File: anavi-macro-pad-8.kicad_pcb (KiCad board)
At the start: 2 copper layers, 40 parts, among them J1 USB_B_Micro, J2 Conn_01x04_Female, J3 Conn_01x03_Male, J4 Conn_01x03_Male, Q1 Q_NPN_BEC, SW1 SW_DIP_x01, SW2 SW_DIP_x01, SW3 SW_DIP_x01, SW4 SW_DIP_x01, SW5 SW_DIP_x01, SW6 SW_DIP_x01, SW7 SW_DIP_x01, SW8 SW_DIP_x01, U1 ATmega32U4-AU, Y1 Crystal

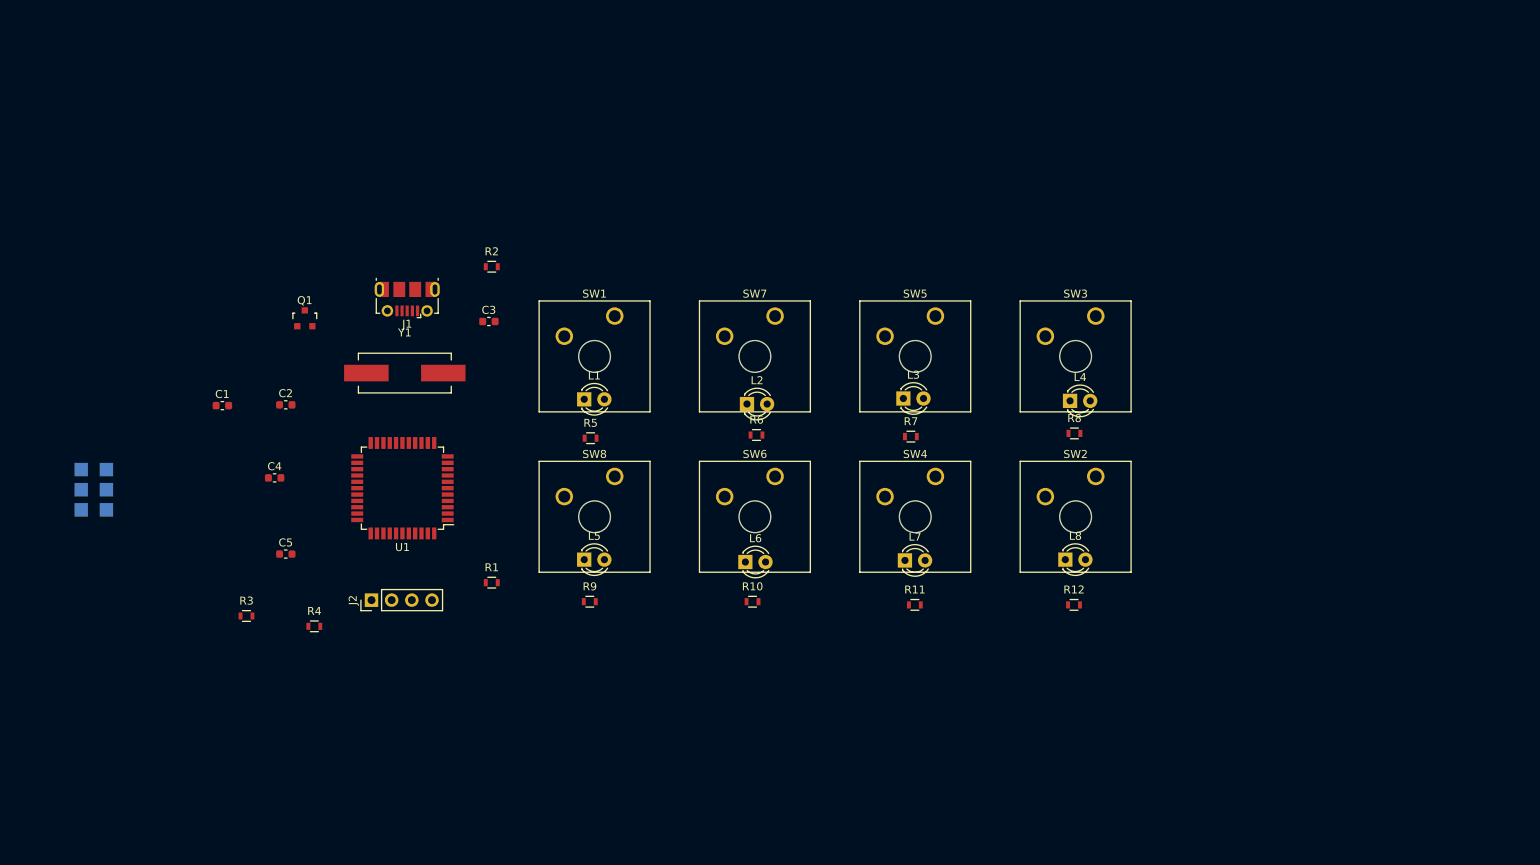
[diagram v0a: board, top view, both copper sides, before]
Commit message: Add outline and arrange components
Signed-off-by: Leon Anavi <leon@anavi.org>
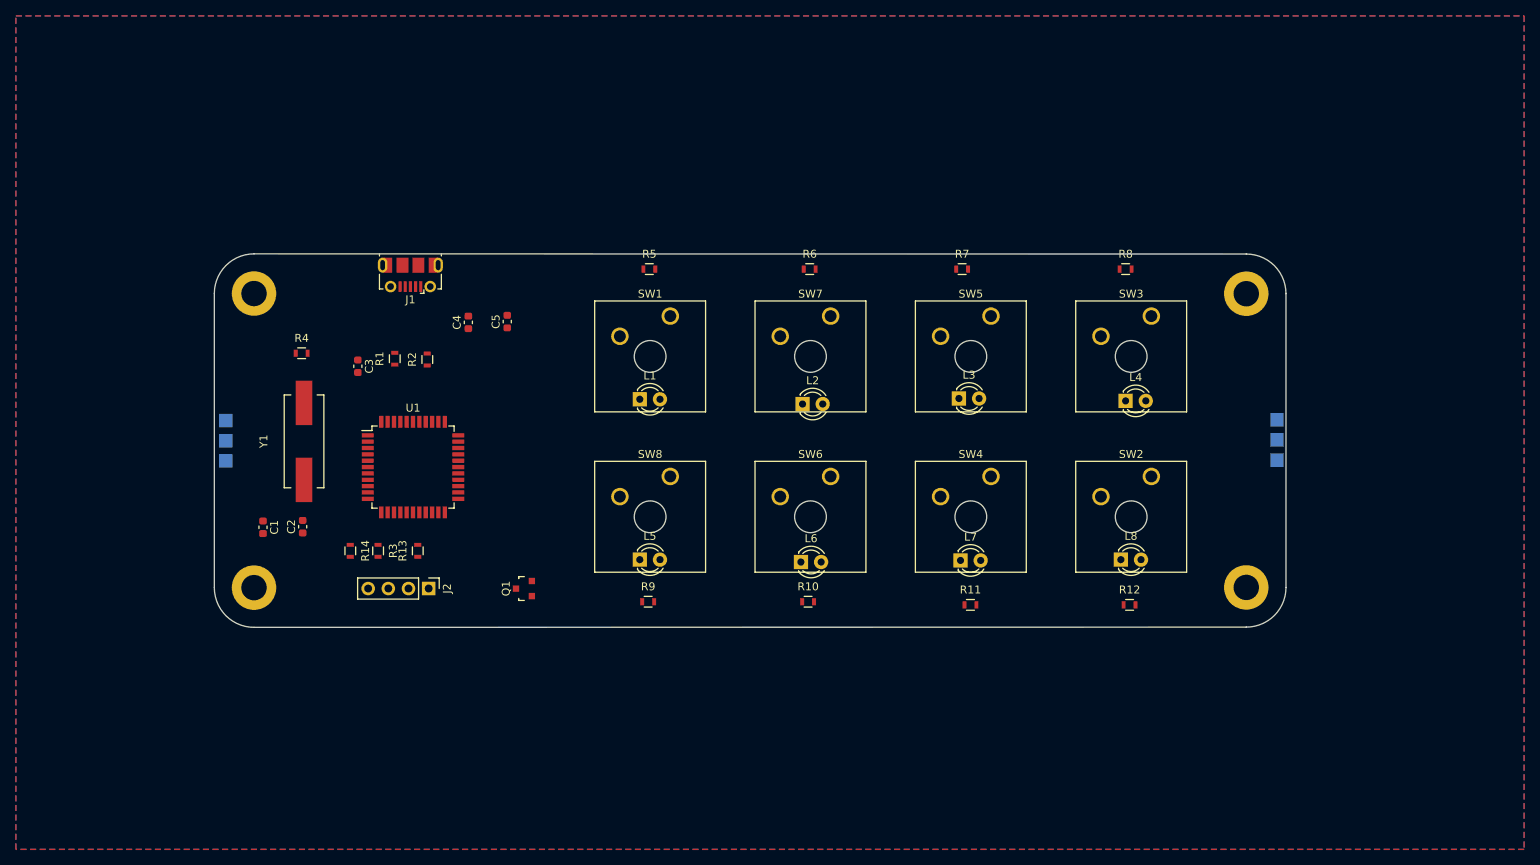
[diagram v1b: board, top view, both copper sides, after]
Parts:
- added R13: 4.7K, Resistors_SMD:R_0603, F.Cu at (70.6, 92.4)
- added R14: 4.7K, Resistors_SMD:R_0603, F.Cu at (62.1, 92.4)
- added REF**: MountingHole_3.2mm_M3_DIN965_Pad, MountingHole:MountingHole_3.2mm_M3_DIN965_Pad, F.Cu at (50.0, 97.0)
- added REF**: MountingHole_3.2mm_M3_DIN965_Pad, MountingHole:MountingHole_3.2mm_M3_DIN965_Pad, F.Cu at (50.0, 60.0)
- added REF**: MountingHole_3.2mm_M3_DIN965_Pad, MountingHole:MountingHole_3.2mm_M3_DIN965_Pad, F.Cu at (175.0, 97.0)
- added REF**: MountingHole_3.2mm_M3_DIN965_Pad, MountingHole:MountingHole_3.2mm_M3_DIN965_Pad, F.Cu at (175.0, 60.0)
- moved J4 147.6 mm to (178.9, 81.0)
- moved Q1 43.8 mm to (84.0, 97.1), turned to 90 degrees
- moved C5 40.4 mm to (81.9, 63.5), turned to 90 degrees
- moved R4 34.4 mm to (56.0, 67.5)
- moved C4 31.3 mm to (77.0, 63.6), turned to 90 degrees
- moved R1 30.7 mm to (67.7, 68.2), turned to 90 degrees
- moved R5 22.5 mm to (99.8, 56.9)
- moved R7 22.1 mm to (139.2, 56.9)
- moved R6 21.9 mm to (120.0, 56.9)
- moved R8 21.7 mm to (159.8, 56.9)
- moved J3 19.2 mm to (46.4, 81.1)
- moved R3 18.5 mm to (65.6, 92.4), turned to 270 degrees
- moved C3 17.4 mm to (63.1, 69.1), turned to 270 degrees
- moved C1 16.2 mm to (51.1, 89.4), turned to 270 degrees
- moved C2 15.5 mm to (56.1, 89.4), turned to 90 degrees
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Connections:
- U1 pad 18: Net-(J2-Pad3) -> Net-(R13-Pad2)
- U1 pad 19: Net-(J2-Pad4) -> Net-(R14-Pad2)
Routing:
- added copper zone on B.Cu, net GND
- added copper zone on F.Cu, net GND
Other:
- board outline added: 135 x 47.1 mm

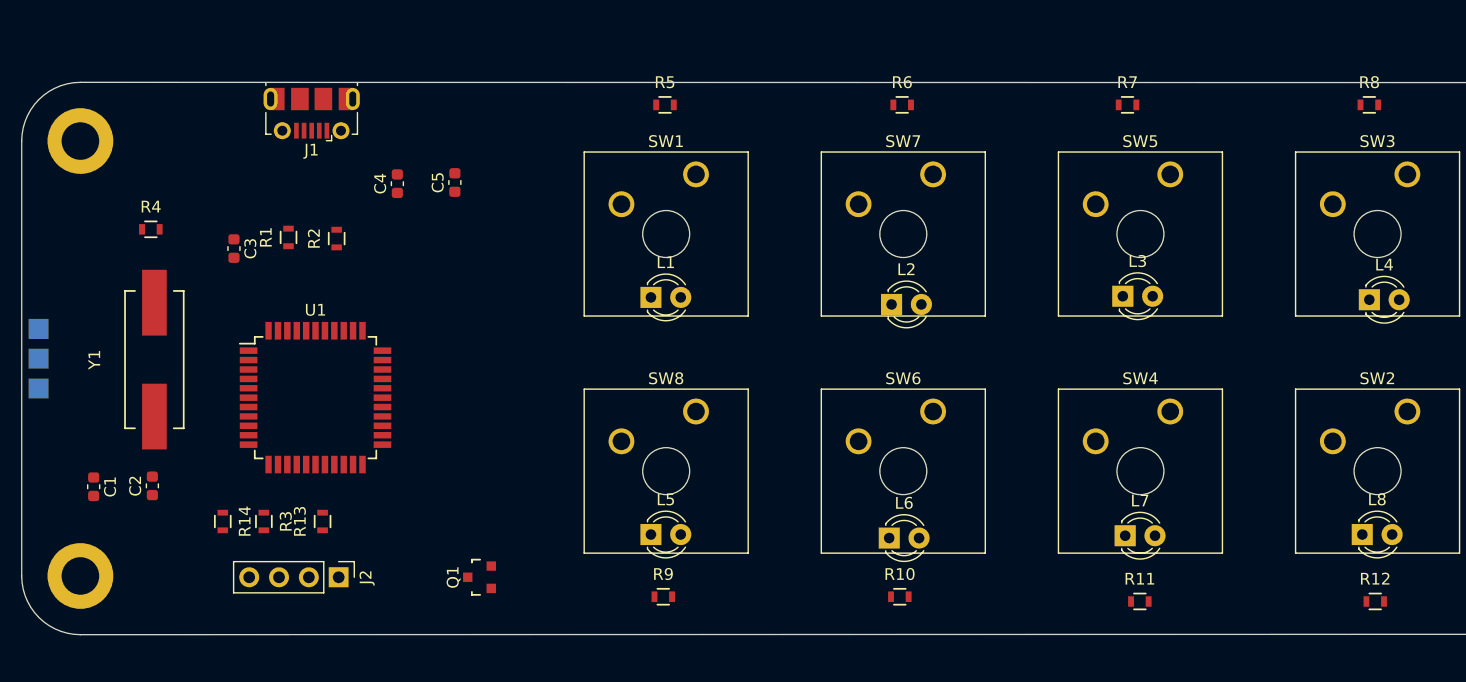
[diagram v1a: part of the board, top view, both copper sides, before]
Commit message: Add components to the schematics
The following modificaitons to the schematics and the PCB have
been done:

* Added RESET button
* Added pins for AVR SPI programmer
* Changed the crystal footprint to 3225
* Minor modificaitons to the PCB layouts

Signed-off-by: Leon Anavi <leon@anavi.org>
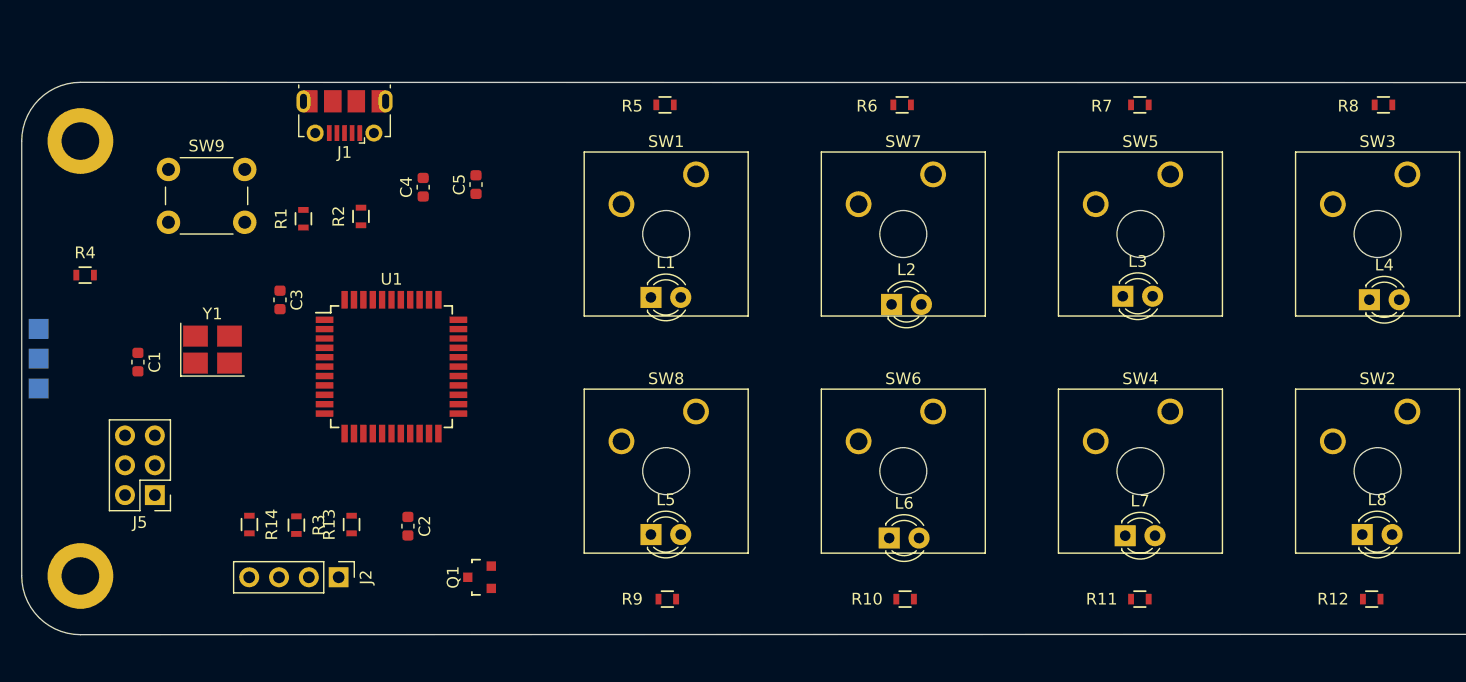
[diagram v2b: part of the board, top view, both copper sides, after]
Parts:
- added J5: AVR-ISP-6, Connector_PinHeader_2.54mm:PinHeader_2x03_P2.54mm_Vertical, F.Cu at (56.3, 90.1)
- added SW9: SW_DIP_x01, Buttons_Switches_ThroughHole:SW_PUSH_6mm_h4.3mm, F.Cu at (57.5, 62.4)
- Y1: footprint Crystals:Crystal_HC49-SD_SMD -> anavi-macro-pad-8:Crystal_SMD_3225-4Pin_3.2x2.5mm_HandSoldering
- moved C2 22.0 mm to (77.9, 92.8), turned to 270 degrees
- moved C1 11.3 mm to (54.9, 78.8)
- moved U1 6.99 mm to (76.5, 79.2)
- moved R4 6.82 mm to (50.4, 71.4)
- moved C3 5.87 mm to (67.0, 73.5)
- moved Y1 5.02 mm to (61.2, 77.8), turned to 0 degrees
- moved J1 2.81 mm to (72.5, 57.8)
- moved R2 2.80 mm to (73.9, 66.4)
- moved R3 2.79 mm to (68.4, 92.7)
- moved R13 2.48 mm to (73.1, 92.7)
- moved R14 2.28 mm to (64.4, 92.7)
- moved C4 2.22 mm to (79.2, 63.9)
- moved R1 2.03 mm to (69.0, 66.6)
- moved C5 1.81 mm to (83.7, 63.7)
- moved R8 1.20 mm to (161.0, 56.9)
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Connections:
- net /RESET renamed Net-(J5-Pad5)
- U1 pad 10: (no net) -> Net-(J5-Pad4)
- U1 pad 11: (no net) -> Net-(J5-Pad1)
- U1 pad 9: (no net) -> Net-(J5-Pad3)

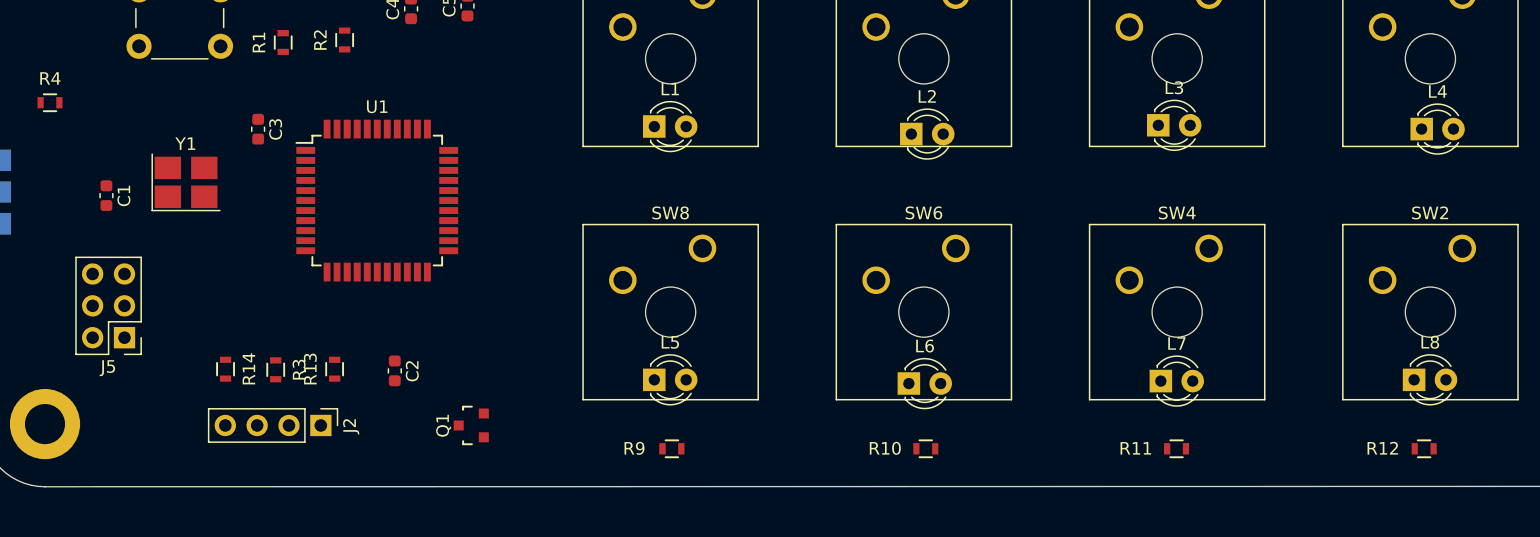
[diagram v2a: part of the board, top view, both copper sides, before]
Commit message: anavi-macro-pad-8.kicad_pcb: Adjust LEDs
Adjust the positions of the AVR SPI Programmer, the backlit
LEDs and the resistors.

Signed-off-by: Leon Anavi <leon@anavi.org>
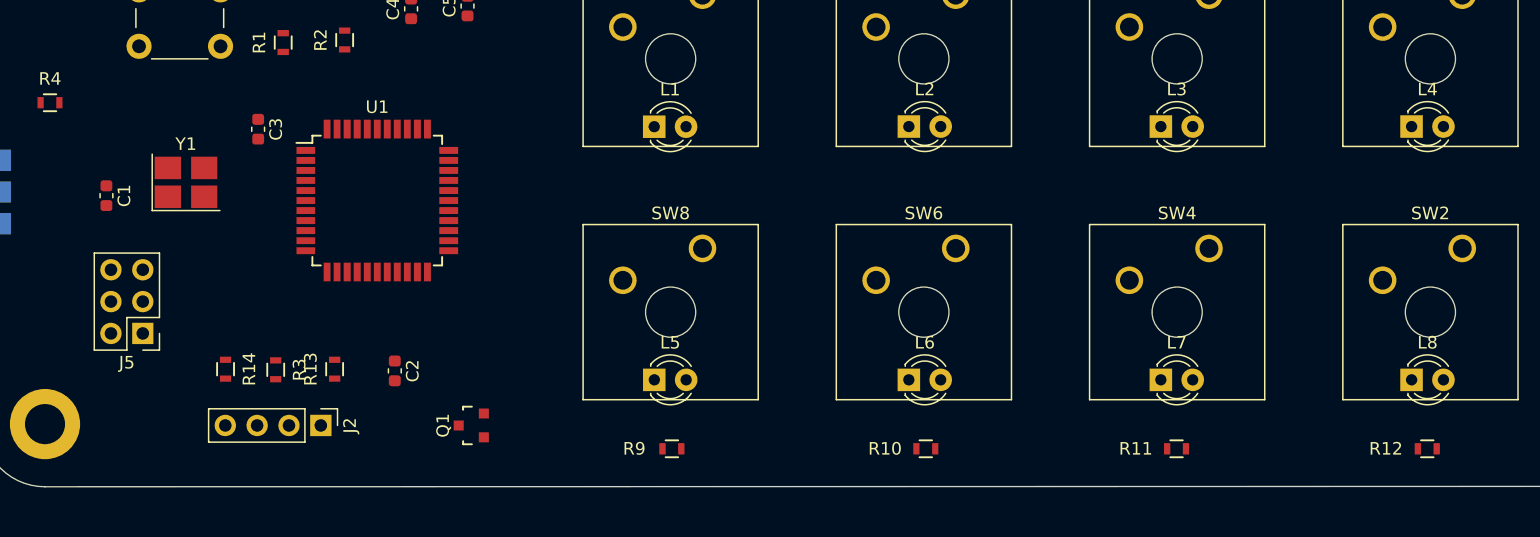
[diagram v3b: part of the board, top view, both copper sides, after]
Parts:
- moved J5 1.50 mm to (57.8, 89.8)
- moved L4 0.82 mm to (159.0, 73.3)
- moved L2 0.63 mm to (118.9, 73.3)
- moved L6 0.30 mm to (118.9, 93.5)
- moved R12 0.25 mm to (160.2, 99.0)
- moved L3 0.22 mm to (139.0, 73.3)
- moved L8 0.20 mm to (159.0, 93.5)
- moved L7 0.10 mm to (139.0, 93.5)
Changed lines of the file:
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@@
   )
   (module LED_THT:LED_D3.0mm (layer F.Cu)
-    (at 98.6 73.3)
+    (at 98.59 73.31)
     (descr "LED, diameter 3.0mm, 2 pins")
     (tags "LED diameter 3.0mm 2 pins")
@@
   )
   (module LED_THT:LED_D3.0mm (layer F.Cu)
-    (at 119.1 73.9)
+    (at 118.9 73.3)
     (descr "LED, diameter 3.0mm, 2 pins")
     (tags "LED diameter 3.0mm 2 pins")
@@
   )
   (module LED_THT:LED_D3.0mm (layer F.Cu)
-    (at 138.8 73.2)
+    (at 139 73.3)
     (descr "LED, diameter 3.0mm, 2 pins")
     (tags "LED diameter 3.0mm 2 pins")
@@
   )
   (module LED_THT:LED_D3.0mm (layer F.Cu)
-    (at 159.8 73.5)
+    (at 159 73.3)
     (descr "LED, diameter 3.0mm, 2 pins")
     (tags "LED diameter 3.0mm 2 pins")
@@
   )
   (module LED_THT:LED_D3.0mm (layer F.Cu)
-    (at 118.9 93.8)
+    (at 118.9 93.5)
     (descr "LED, diameter 3.0mm, 2 pins")
     (tags "LED diameter 3.0mm 2 pins")
@@
   )
   (module LED_THT:LED_D3.0mm (layer F.Cu)
-    (at 139 93.6)
+    (at 139 93.5)
     (descr "LED, diameter 3.0mm, 2 pins")
     (tags "LED diameter 3.0mm 2 pins")
@@
   )
   (module LED_THT:LED_D3.0mm (layer F.Cu)
-    (at 159.2 93.5)
+    (at 159 93.5)
     (descr "LED, diameter 3.0mm, 2 pins")
     (tags "LED diameter 3.0mm 2 pins")
@@
   )
   (module Resistors_SMD:R_0603 (layer F.Cu)
-    (at 160 99)
+    (at 160.25 99)
     (descr "Resistor SMD 0603, reflow soldering, Vishay (see dcrcw.pdf)")
     (tags "resistor 0603")
@@
       (effects (font (size 1 1) (thickness 0.15)) (justify mirror))
     )
-    (fp_text value Conn_01x03_Male (at 0 -7.62 -180) (layer B.Fab)
+    (fp_text value Conn_01x03_Male (at 0 -7.62 -180) (layer B.Fab) hide
       (effects (font (size 1 1) (thickness 0.15)) (justify mirror))
     )
@@
       (effects (font (size 1 1) (thickness 0.15)) (justify mirror))
     )
-    (fp_text value Conn_01x03_Male (at 0 -7.62 -180) (layer B.Fab)
+    (fp_text value Conn_01x03_Male (at 0 -7.62 -180) (layer B.Fab) hide
       (effects (font (size 1 1) (thickness 0.15)) (justify mirror))
     )
@@
   )
   (module Connector_PinHeader_2.54mm:PinHeader_2x03_P2.54mm_Vertical (layer F.Cu)
-    (at 56.34 90.14 180)
+    (at 57.8 89.8 180)
     (descr "Through hole straight pin header, 2x03, 2.54mm pitch, double rows")
     (tags "Through hole pin header THT 2x03 2.54mm double row")
